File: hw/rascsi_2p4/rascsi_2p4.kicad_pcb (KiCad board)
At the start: 2 copper layers, 65 x 56 mm, 98 parts, among them J1 Raspberry_Pi_2_3, J10 Conn_01x04_Male, J2 DNP, J20 171826-4, J3 Conn_02x25_Odd_Even, J4 I2C Pinout, J5 DNP, J6 CONNFLY DB-25, J7 DNP, J8 USB_B_Micro, J9 Conn_02x25_Odd_Even, U1 74ALVC164245DGG, U2 74ALVC164245DGG, U3 UCC5606PWPTR, U4 UCC5606PWPTR, X1 Mac, X3 Mac, X7 Pi, X8 Pi

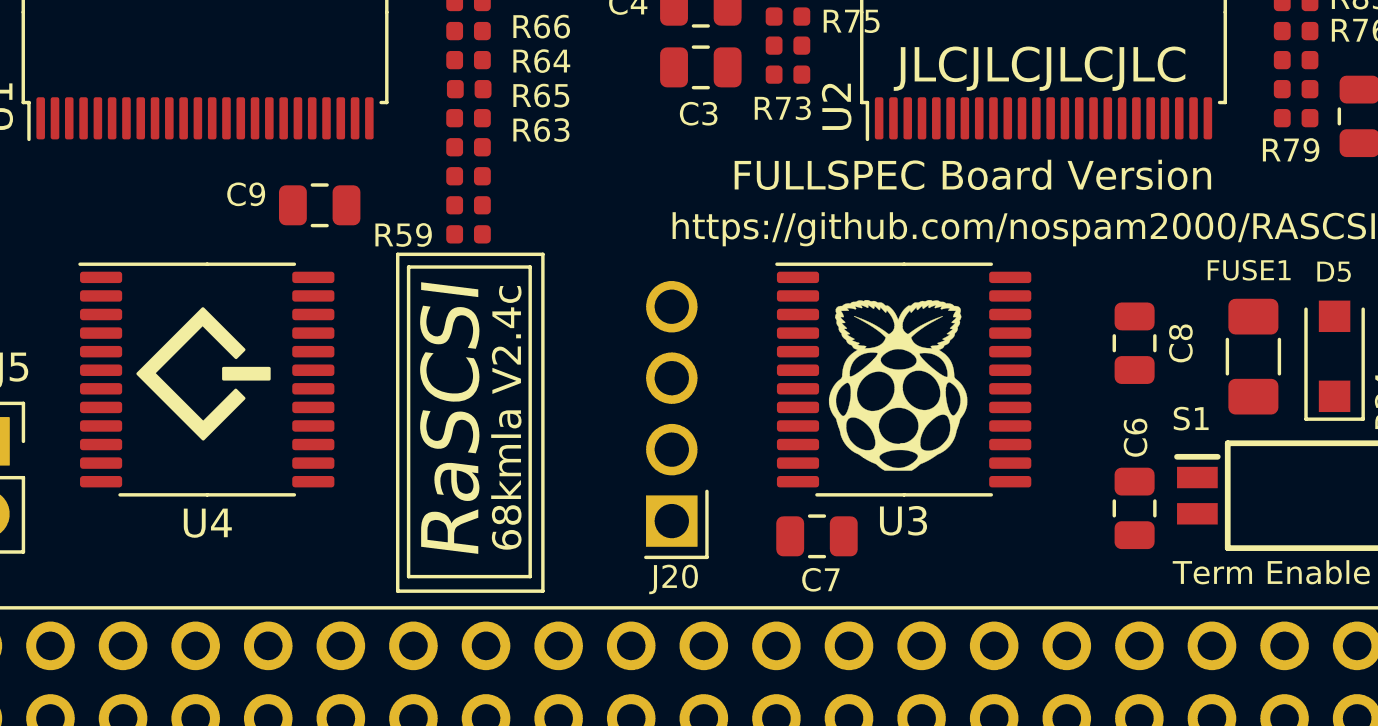
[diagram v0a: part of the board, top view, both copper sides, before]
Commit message: moved C9 and C8 for successful routing
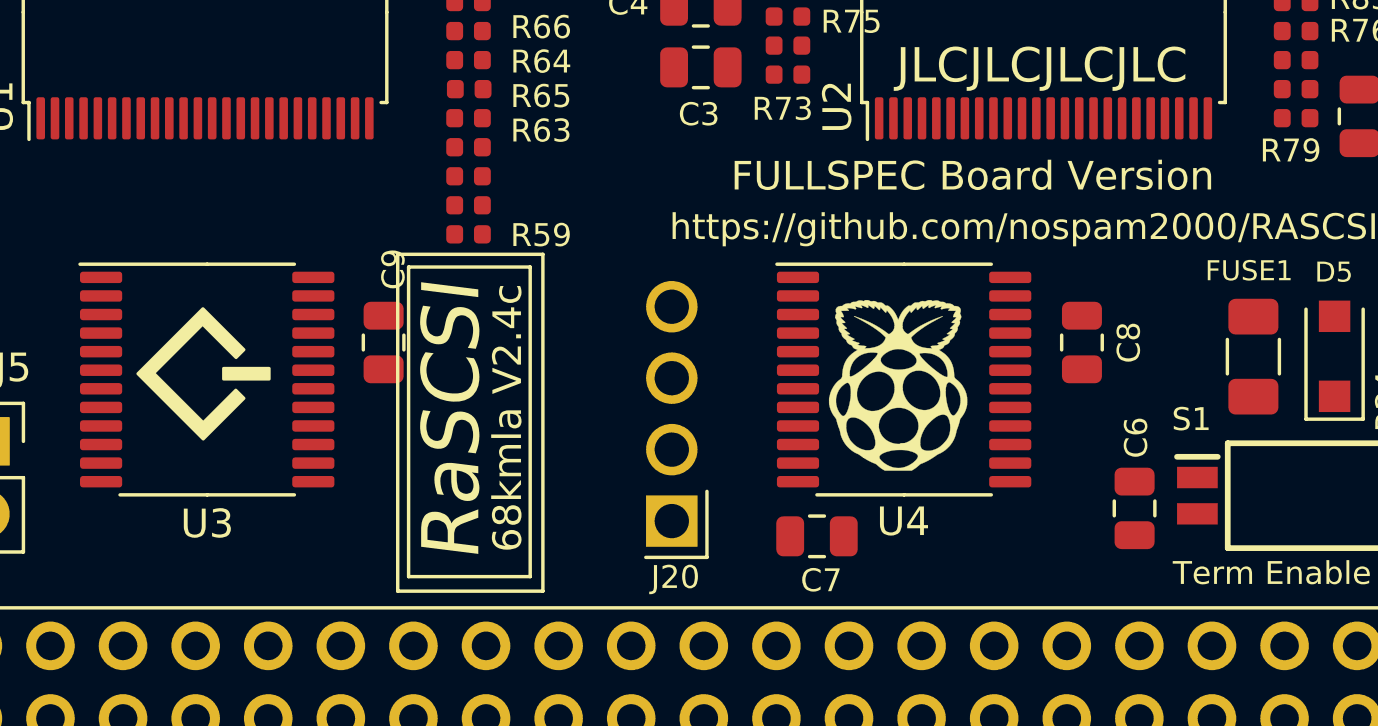
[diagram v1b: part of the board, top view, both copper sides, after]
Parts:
- moved C9 5.30 mm to (195.7, 69.8), turned to 270 degrees
- moved C8 1.84 mm to (220.2, 69.8)
- renumbered U4 to U3, U3 to U4
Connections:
- U3 pad 1: C-C_D -> C-D4
- U3 pad 12: C-ATN -> C-D7
- U3 pad 13: C-ACK -> C-D3
- U3 pad 14: C-RST -> C-D2
- U3 pad 15: C-SEL -> C-D1
- U3 pad 2: C-REQ -> C-D5
- U3 pad 23: C-BSY -> C-D0
- U3 pad 24: C-MSG -> C-DP
- U3 pad 3: C-I_O -> C-D6
- U4 pad 1: C-D6 -> C-BSY
- U4 pad 12: C-D0 -> C-REQ
- U4 pad 13: C-D1 -> C-I_O
- U4 pad 14: C-D2 -> C-ATN
- U4 pad 15: C-D3 -> C-ACK
- U4 pad 2: C-D7 -> C-MSG
- U4 pad 23: C-D4 -> C-RST
- U4 pad 24: C-D5 -> C-SEL
- U4 pad 3: C-DP -> C-C_D

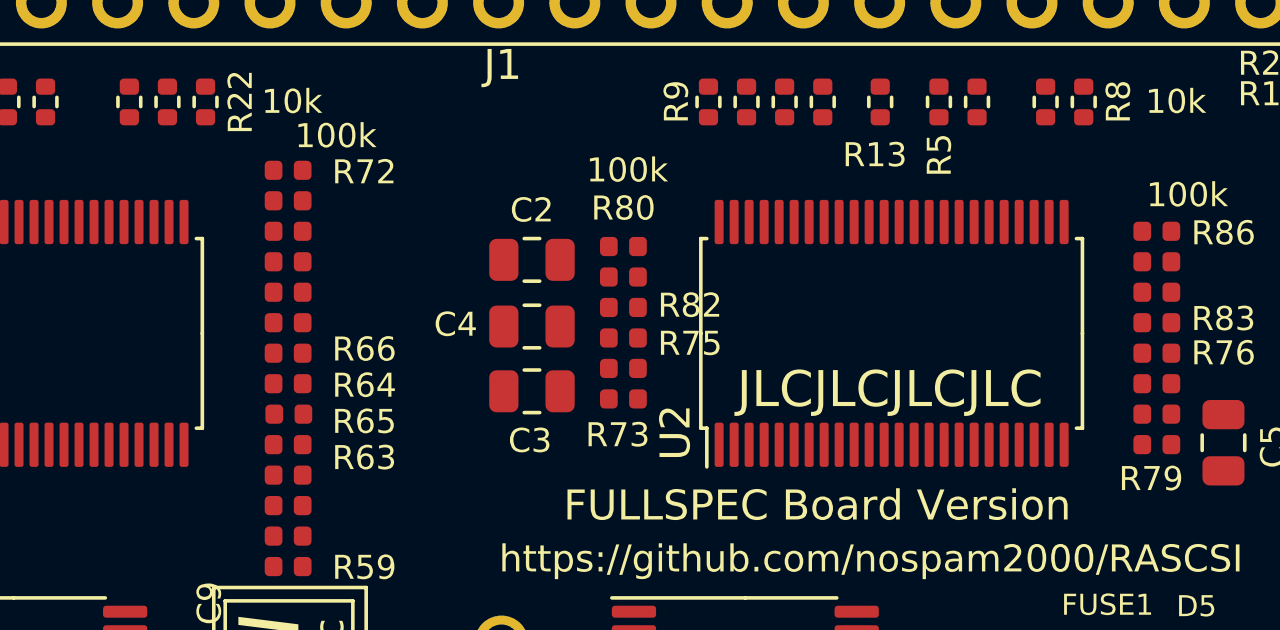
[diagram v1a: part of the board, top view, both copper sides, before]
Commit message: added NarrowPowerAdapter to easy routing
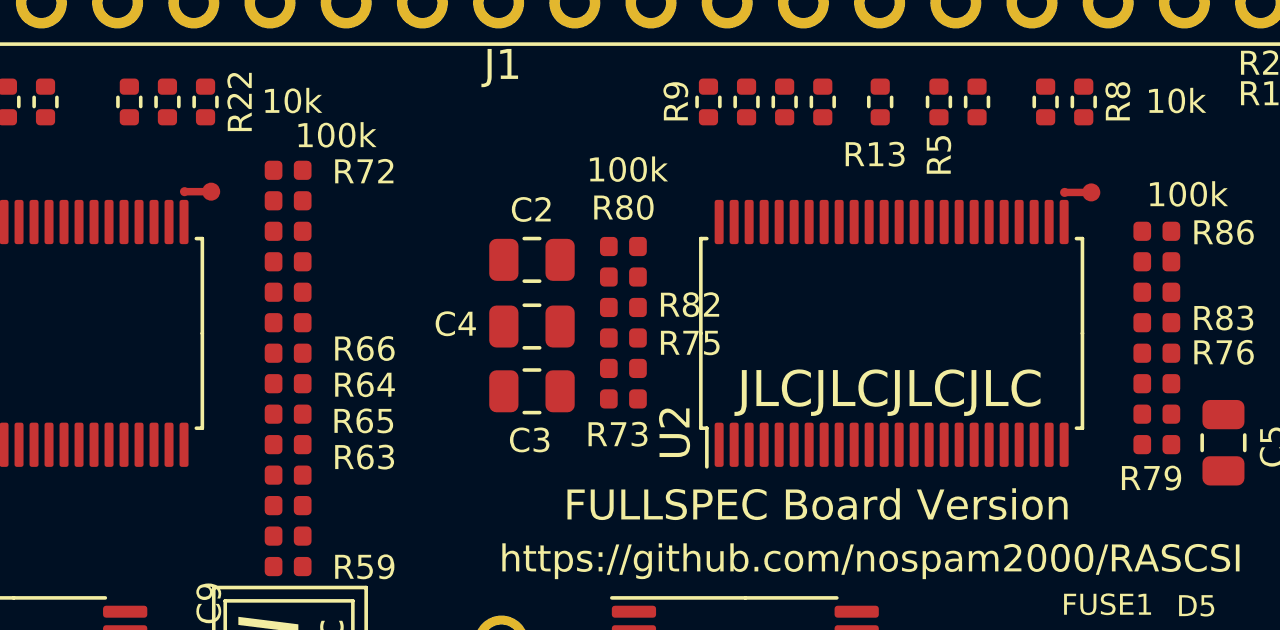
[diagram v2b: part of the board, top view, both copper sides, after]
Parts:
- added U5: NarrowPowerAdapter, amiga:NarrowPowerAdapter_0.60_to_0.25, F.Cu at (196.1, 53.6)
- added U6: NarrowPowerAdapter, amiga:NarrowPowerAdapter_0.60_to_0.25, F.Cu at (225.5, 53.6)
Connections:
- U1 pad 21: GND -> GND_U1_A
- U1 pad 25: GND -> GND_U1_A
- U1 pad 28: GND -> GND_U1_A
- U2 pad 25: GND -> GND_U2_A
- U2 pad 28: GND -> GND_U2_A
- U3 pad 1: C-D4 -> C-D7
- U3 pad 12: C-D7 -> C-D4
- U3 pad 2: C-D5 -> C-D6
- U3 pad 3: C-D6 -> C-D5

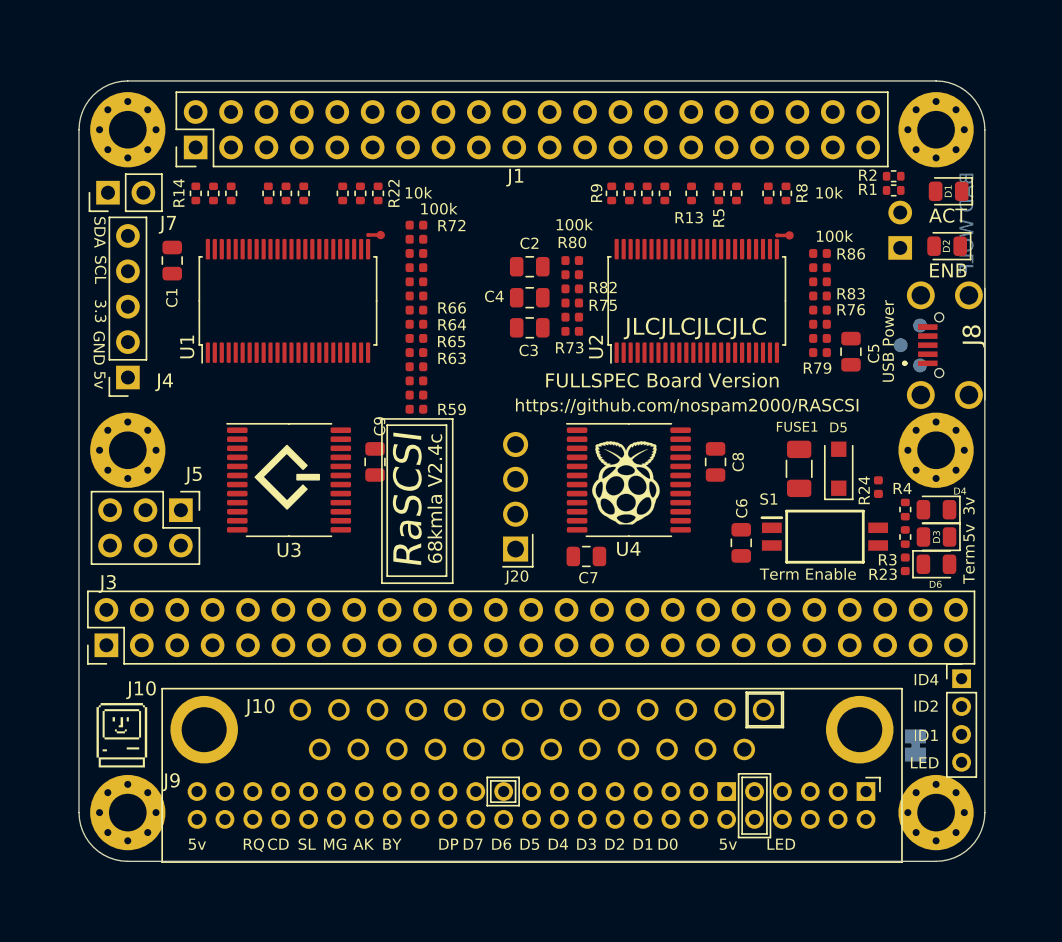
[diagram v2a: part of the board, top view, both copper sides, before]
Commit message: imported routing result with 96 vias
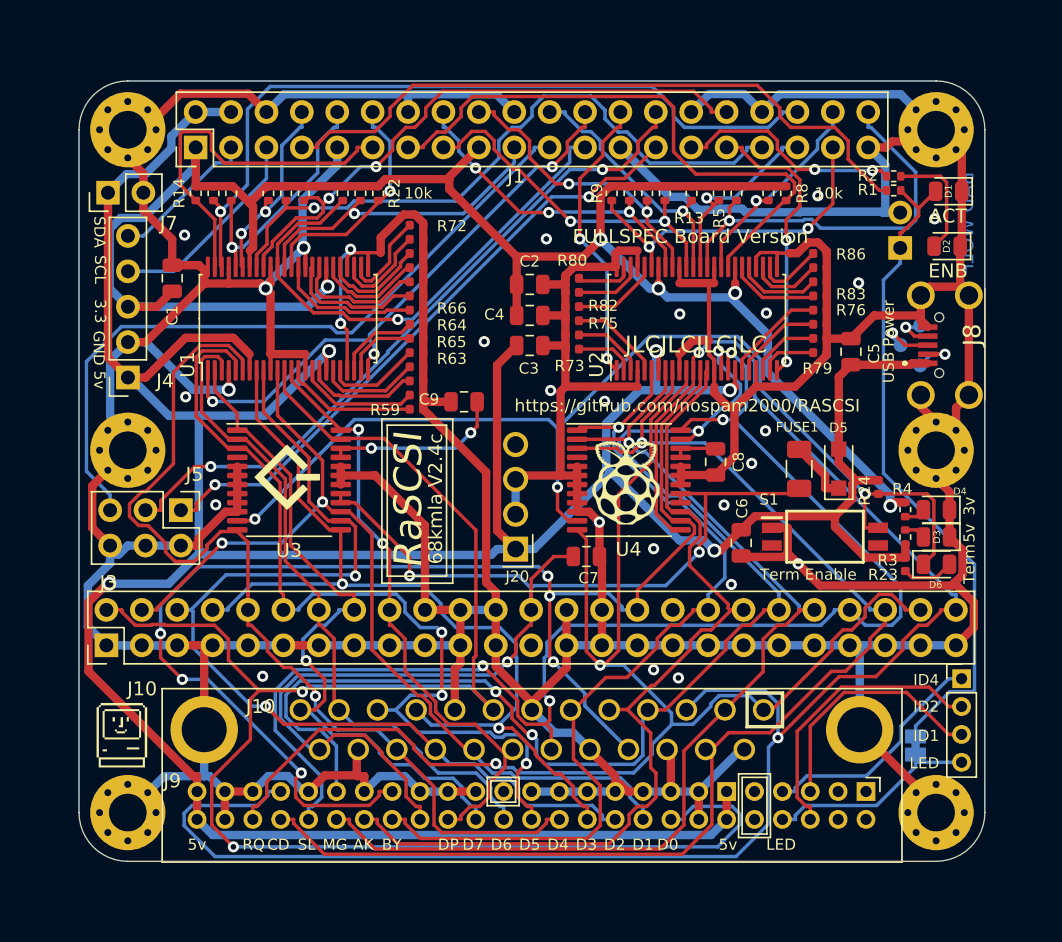
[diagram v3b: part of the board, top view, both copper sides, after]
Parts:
- moved C9 7.71 mm to (202.1, 65.5), turned to 180 degrees
- moved U5 1.27 mm to (196.1, 54.8)
- moved U6 1.27 mm to (225.5, 54.9)
- moved C1 1.27 mm to (181.2, 56.7)
- moved C3 1.27 mm to (206.8, 59.3)
- moved C4 1.27 mm to (206.8, 61.5)
- moved R74 1.27 mm to (209.9, 60.7)
- moved R75 1.27 mm to (209.9, 59.7)
- moved R80 1.27 mm to (209.9, 56.7)
- moved U1 1.27 mm to (189.5, 59.6)
- moved U2 1.27 mm to (218.8, 59.6)
- moved C2 1.27 mm to (206.8, 57.1)
- moved R73 1.27 mm to (209.9, 61.7)
- moved R81 1.27 mm to (209.9, 57.7)
- moved R82 1.27 mm to (209.9, 58.7)
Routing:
- net GND: track 0.00 -> 644.0 mm, vias 0 -> 25
- net +5V: track 0.00 -> 249.2 mm, vias 0 -> 5
- net +3V3: track 0.00 -> 136.5 mm, vias 0 -> 5
- net C-I_O: track 0.00 -> 129.9 mm, vias 0 -> 2
- net C-D0: track 0.00 -> 121.8 mm, vias 0 -> 2
- net C-REQ: track 0.00 -> 102.8 mm, vias 0 -> 2
- net C-ATN: track 0.00 -> 99.7 mm, vias 0 -> 6
- net C-SEL: track 0.00 -> 99.3 mm, vias 0 -> 4
- net TERMPOW: track 0.00 -> 90.7 mm, vias 0 -> 3
- net C-C_D: track 0.00 -> 90.1 mm, vias 0 -> 1
- net C-RST: track 0.00 -> 89.8 mm, vias 0 -> 4
- net ~TERM_ENABLE: track 0.00 -> 78.0 mm, vias 0 -> 3
- net C-MSG: track 0.00 -> 75.5 mm, vias 0 -> 1
- net C-D2: track 0.00 -> 71.0 mm, vias 0 -> 2
- net C-D4: track 0.00 -> 68.2 mm, vias 0 -> 1
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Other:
- board text removed: "100k"

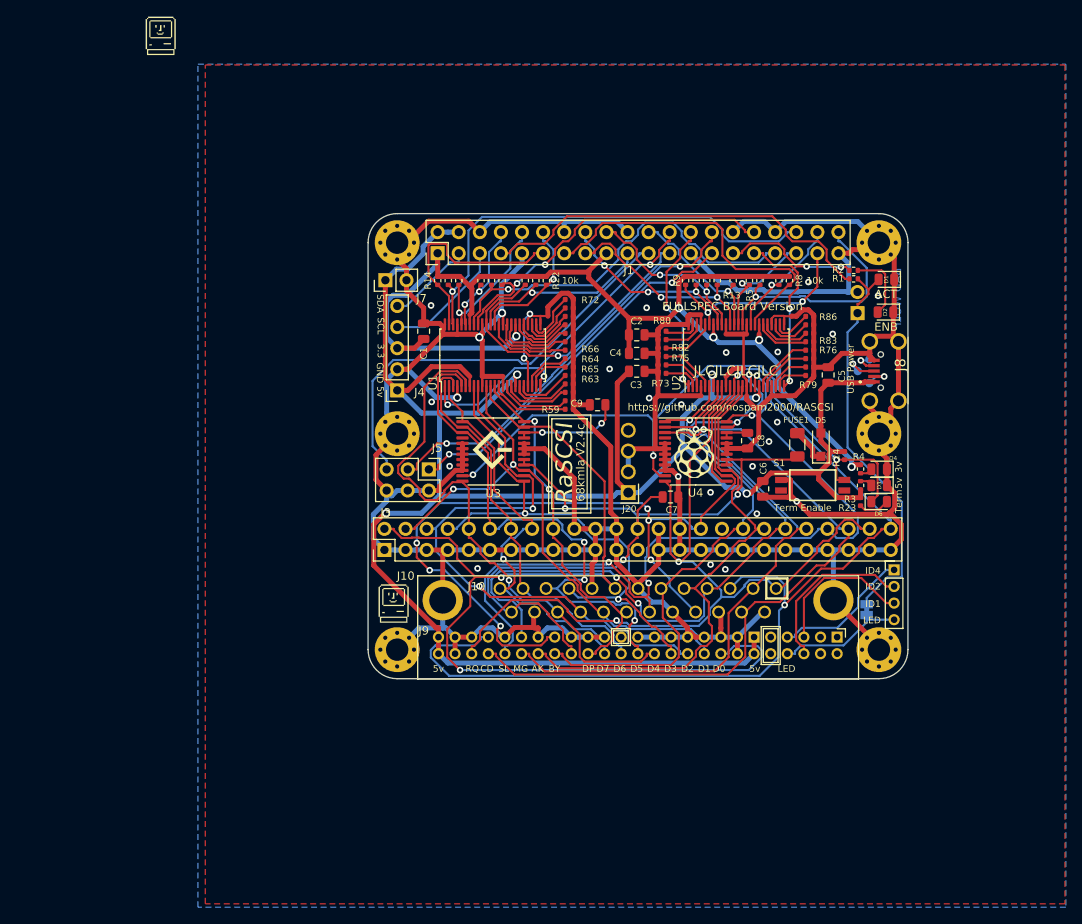
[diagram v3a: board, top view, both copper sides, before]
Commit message: first routable version
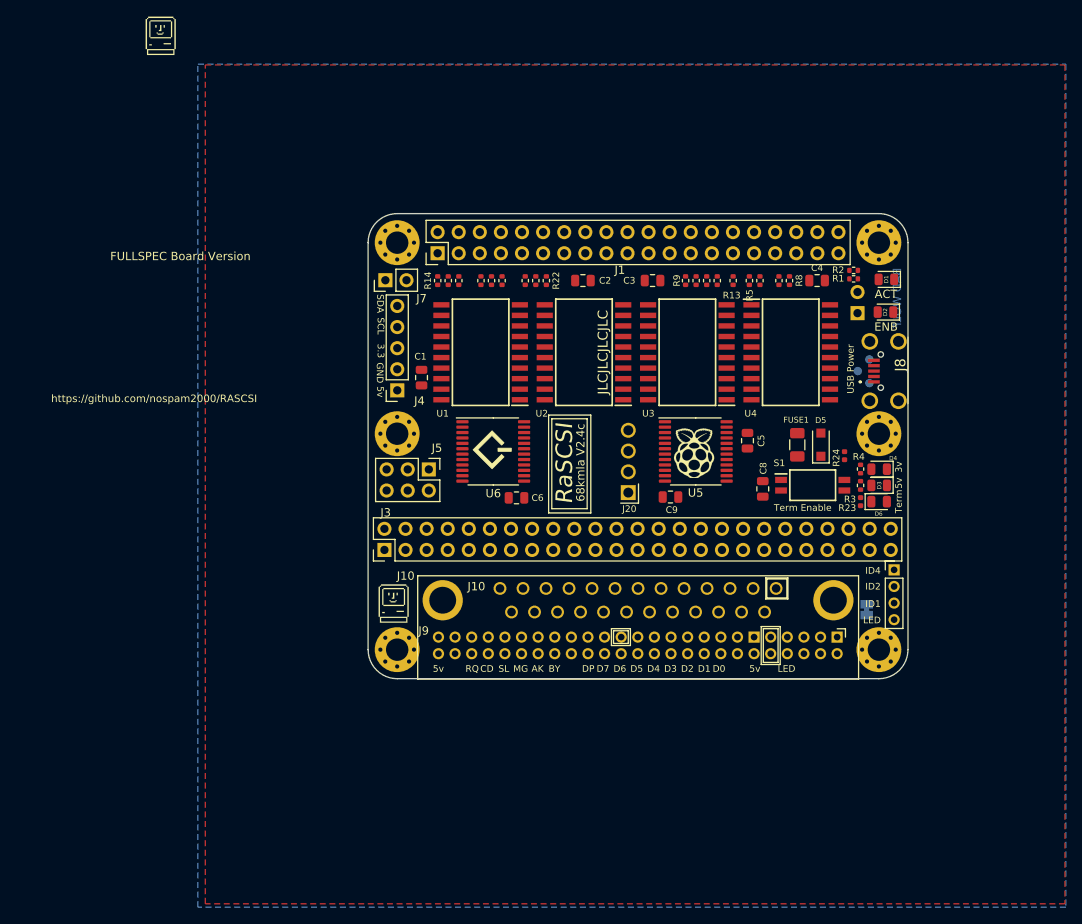
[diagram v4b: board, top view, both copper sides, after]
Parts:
- removed the C5 at (229.9, 61.9)
- removed R59, R60, R61, R62, R63, R64, R65, R66, R67, R68, R69, R70, R71, R72, R73, R74, R75, R76, R77, R78, R79, R80, R81, R82, R83, R84, R85, R86: 100k, Resistor_SMD:R_0402_1005Metric
- removed the U5 at (196.1, 54.8)
- removed the U6 at (225.5, 54.9)
- added U3: SN74LS641-1DW, SamacSys_Parts:SOIC127P1030X265-20N, F.Cu at (212.9, 59.2)
- added U4: SN74LS641-1DW, SamacSys_Parts:SOIC127P1030X265-20N, F.Cu at (225.4, 59.2)
- C3: value 10u -> 330n
- U1, U2: value 74ALVC164245DGG -> SN74LS641-1DW; footprint Package_SO:TSSOP-48_6.1x12.5mm_P0.5mm -> SamacSys_Parts:SOIC127P1030X265-20N
- moved C4 24.3 mm to (228.6, 50.6)
- moved U2 18.3 mm to (200.5, 59.2), turned to 180 degrees
- moved C6 14.9 mm to (192.4, 76.7)
- moved C2 9.20 mm to (200.4, 50.6)
- moved C3 8.97 mm to (208.7, 50.6), turned to 180 degrees
- moved C1 5.59 mm to (180.9, 62.2)
- moved U1 1.49 mm to (188.0, 59.2), turned to 180 degrees
- renumbered C8 to C5, C9 to C6, C6 to C8, C7 to C9, U4 to U5, U3 to U6
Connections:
- C1 pad 1: +3V3 -> +5V
- C2 pad 1: +3V3 -> +5V
- C3 pad 1: +3V3 -> +5V
- U1 pad 11: C-D1 -> PI-D0
- U1 pad 12: C-D0 -> PI-D1
- U1 pad 13: C-DP -> PI-D2
- U1 pad 14: PULLDOWN1 -> PI-D3
- U1 pad 15: GND -> PI-D4
- U1 pad 16: PULLDOWN2 -> PI-D5
- U1 pad 17: PULLDOWN3 -> PI-D6
- U1 pad 18: +5V -> PI-D7
- U1 pad 19: PULLDOWN4 -> GND
- U1 pad 20: PULLDOWN5 -> +5V
- U1 pad 4: GND -> C-D5
- U1 pad 5: C-D5 -> C-D4
- U1 pad 6: C-D4 -> C-D3
- U1 pad 7: +5V -> C-D2
- U1 pad 8: C-D3 -> C-D1
- U1 pad 9: C-D2 -> C-D0
- U2 pad 1: PI-TAD -> PI-DTD
- U2 pad 11: C-REQ -> GND
- U2 pad 12: C-I_O -> GND
- U2 pad 13: C-ATN -> GND
- U2 pad 14: C-ACK -> GND
- U2 pad 16: C-RST -> GND
- U2 pad 17: C-SEL -> GND
- U2 pad 18: +5V -> PI-DP
- U2 pad 19: PULLDOWN18 -> GND
- U2 pad 2: PULLDOWN15 -> C-DP
- U2 pad 20: PULLDOWN19 -> +5V
- U2 pad 3: PULLDOWN16 -> GND
- U2 pad 5: PULLDOWN17 -> GND
- U2 pad 6: C-BSY -> GND
- U2 pad 7: +5V -> GND
- U2 pad 8: C-MSG -> GND
- U2 pad 9: C-C_D -> GND
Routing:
- net GND: track 644.0 -> 0.00 mm, vias 25 -> 0
- net +5V: track 249.2 -> 0.00 mm, vias 5 -> 0
- net +3V3: track 136.5 -> 0.00 mm, vias 5 -> 0
- net C-I_O: track 129.9 -> 0.00 mm, vias 2 -> 0
- net C-D0: track 121.8 -> 0.00 mm, vias 2 -> 0
- net C-REQ: track 102.8 -> 0.00 mm, vias 2 -> 0
- net C-ATN: track 99.7 -> 0.00 mm, vias 6 -> 0
- net C-SEL: track 99.3 -> 0.00 mm, vias 4 -> 0
- net TERMPOW: track 90.7 -> 0.00 mm, vias 3 -> 0
- net C-C_D: track 90.1 -> 0.00 mm, vias 1 -> 0
- net C-RST: track 89.8 -> 0.00 mm, vias 4 -> 0
- net ~TERM_ENABLE: track 78.0 -> 0.00 mm, vias 3 -> 0
- net C-MSG: track 75.5 -> 0.00 mm, vias 1 -> 0
- net C-D2: track 71.0 -> 0.00 mm, vias 2 -> 0
- net C-D4: track 68.2 -> 0.00 mm, vias 1 -> 0
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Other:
- board text removed: "10k"
